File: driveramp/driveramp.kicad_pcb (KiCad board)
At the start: 2 copper layers, 17 parts, among them J1 SMA, J2 SMA, Q1 MRFE6VS25L

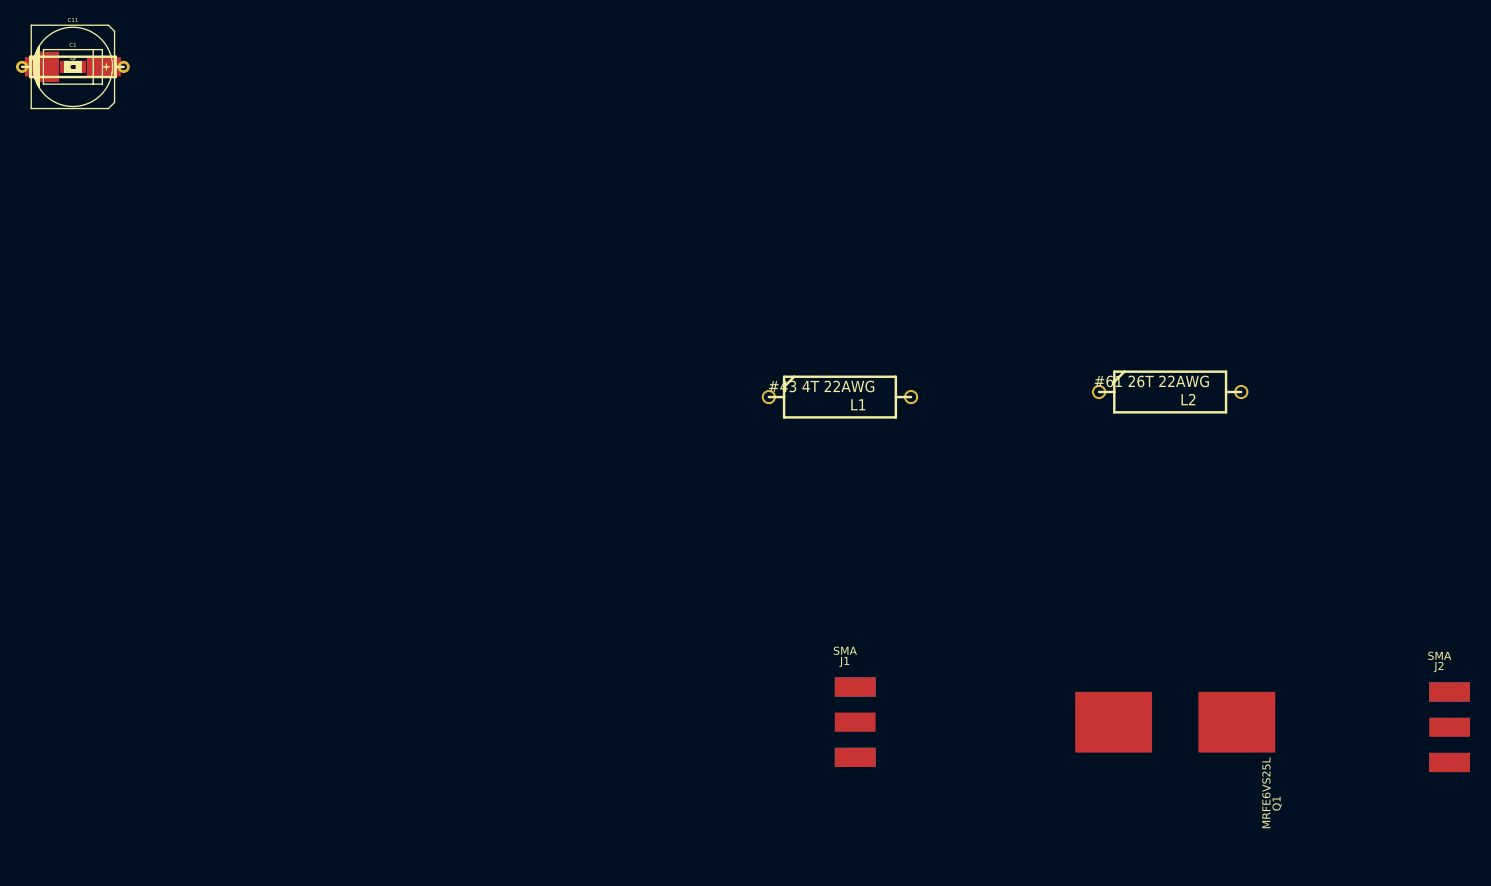
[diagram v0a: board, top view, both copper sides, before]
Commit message: modified trace width classes
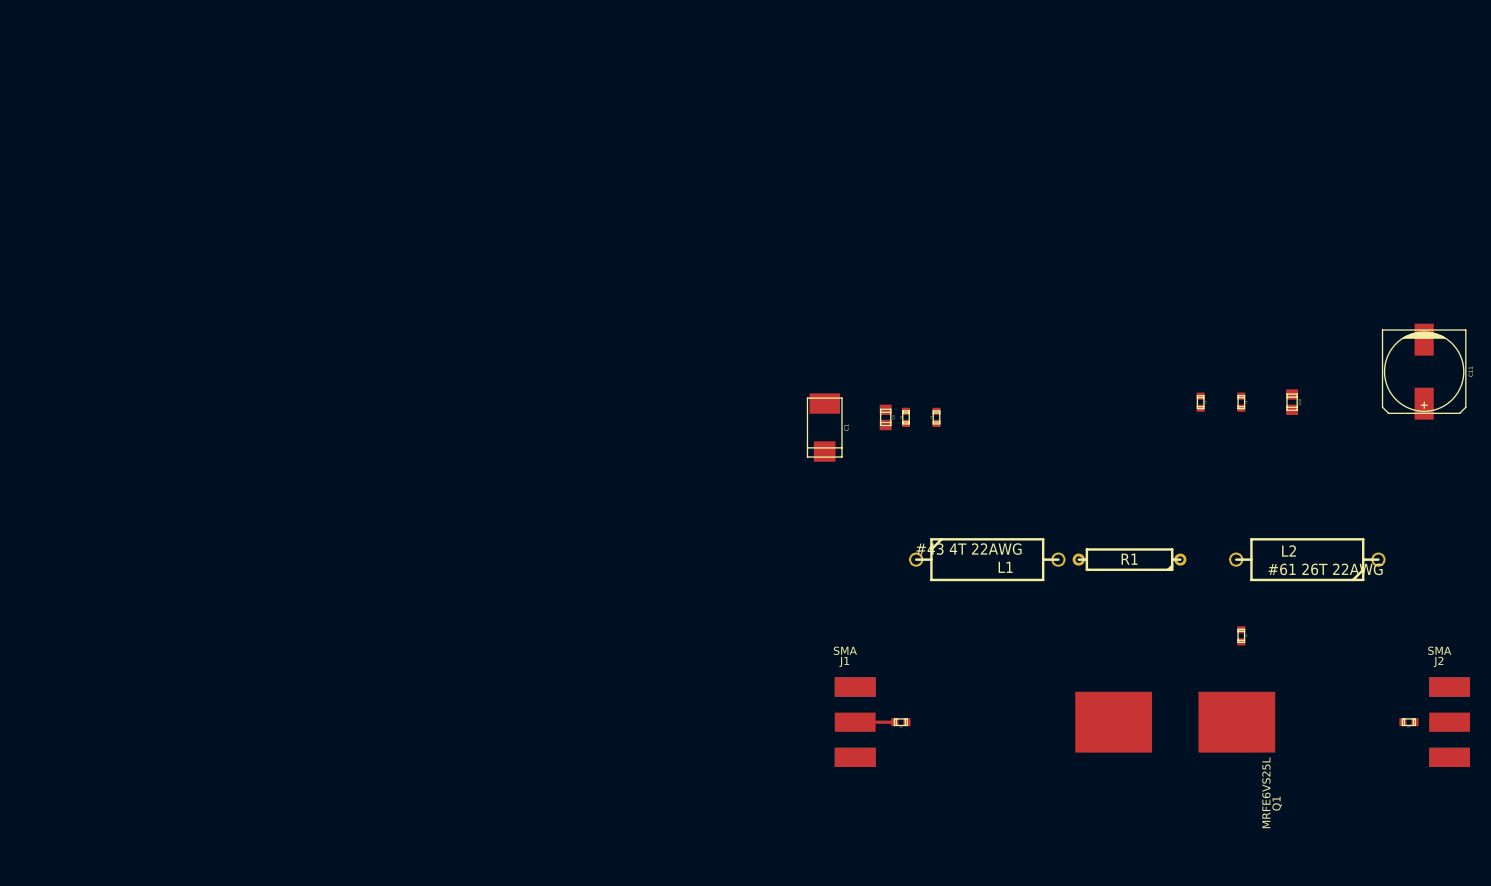
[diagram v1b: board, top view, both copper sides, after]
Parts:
- moved C7 186.0 mm to (167.0, 81.9), turned to 180 degrees
- moved C11 173.2 mm to (168.9, 38.1), turned to 270 degrees
- moved C6 162.4 mm to (146.1, 71.1), turned to 270 degrees
- moved C10 158.1 mm to (152.4, 41.9), turned to 270 degrees
- moved C8 151.9 mm to (146.1, 41.9), turned to 270 degrees
- moved C9 147.1 mm to (141.0, 41.9), turned to 270 degrees
- moved R1 145.7 mm to (132.1, 61.6), turned to 180 degrees
- moved C5 132.0 mm to (103.5, 81.9), turned to 180 degrees
- moved C4 116.5 mm to (108.0, 43.8), turned to 90 degrees
- moved C2 113.0 mm to (104.1, 43.8), turned to 90 degrees
- moved C3 110.6 mm to (101.6, 43.8), turned to 270 degrees
- moved C1 104.2 mm to (94.0, 45.1), turned to 270 degrees
- moved L1 27.4 mm to (114.3, 61.6)
- moved L2 27.1 mm to (154.3, 61.6), turned to 180 degrees
- moved J2 0.63 mm to (172.1, 81.9)
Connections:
- net N-000004 renamed /vbias
- C10 pad 1: N-000003 (its old number) -> /vsupply
- C11 pad 1: N-000003 (its old number) -> /vsupply
- C8 pad 1: N-000003 (its old number) -> /vsupply
- C9 pad 1: N-000003 (its old number) -> /vsupply
- L2 pad 1: N-000003 (its old number) -> /vsupply
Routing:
- net N-000001: track 0.00 -> 4.96 mm
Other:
- copper layers 2 -> 4
- net class 50 Ohm added: clearance 0.8, trace_width 0.4, via_dia 0.889, via_drill 0.635
- net class MRF Feed added: clearance 0.254, trace_width 1.6, via_dia 0.889, via_drill 0.635
- net class Power added: clearance 0.254, trace_width 2, via_dia 0.889, via_drill 0.635

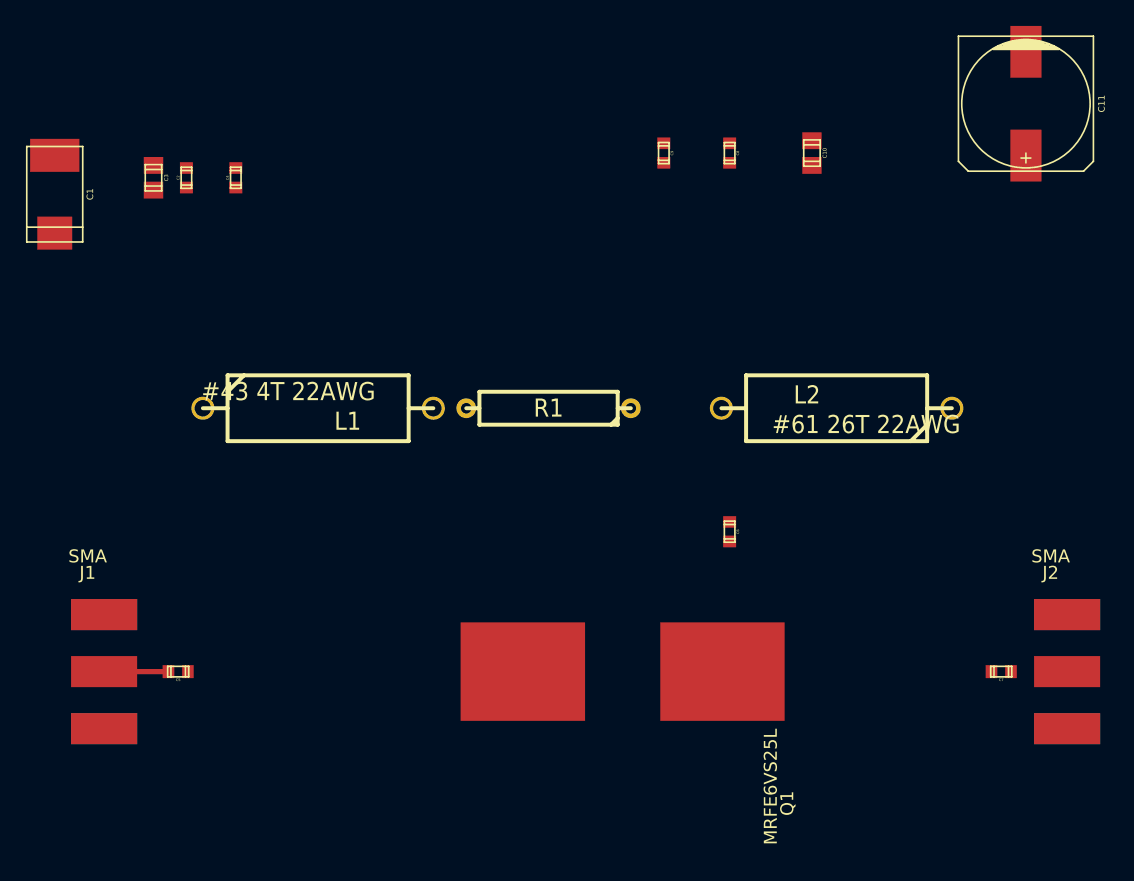
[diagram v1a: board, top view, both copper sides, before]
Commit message: component placement
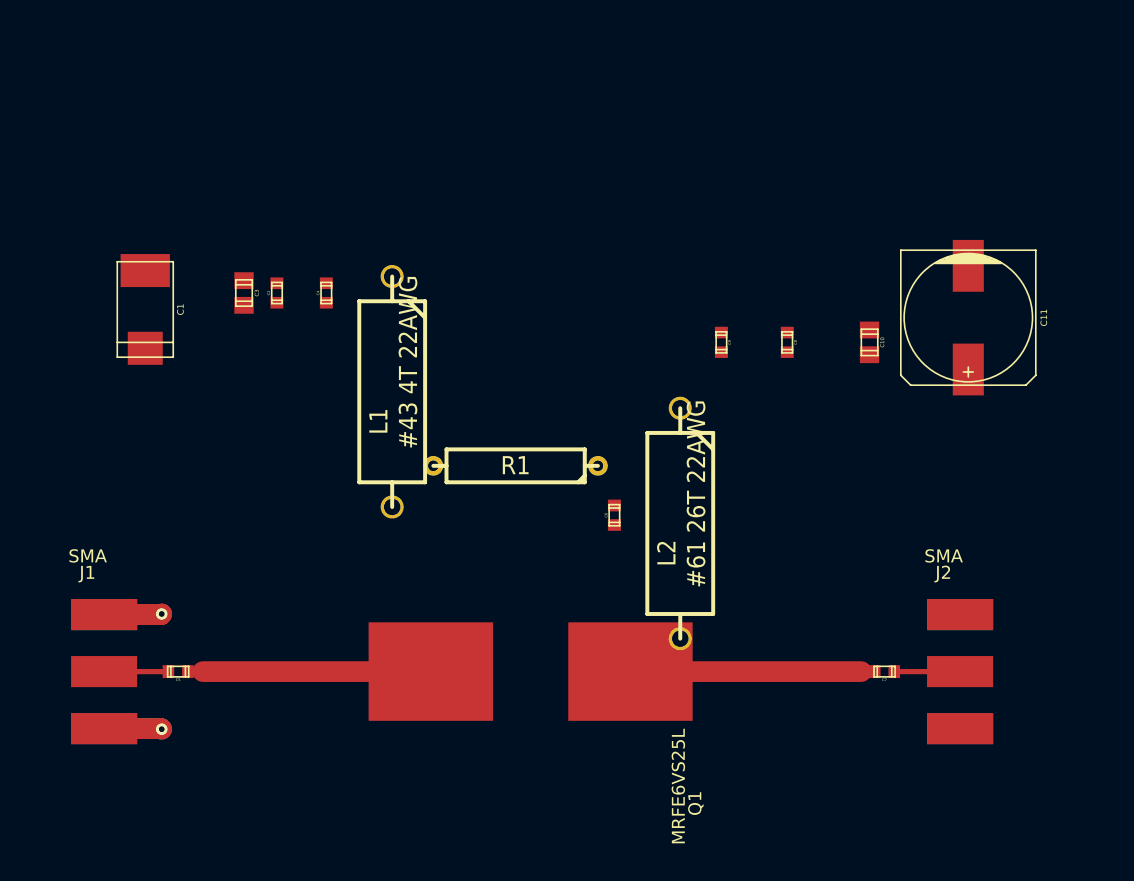
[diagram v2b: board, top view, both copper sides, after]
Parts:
- moved C11 17.1 mm to (164.5, 54.6)
- moved C10 15.3 mm to (156.8, 56.5)
- moved C8 15.3 mm to (150.5, 56.5)
- moved C9 15.3 mm to (145.4, 56.5)
- moved L2 15.0 mm to (142.2, 70.5), turned to 270 degrees
- moved C1 11.3 mm to (101.0, 54.0)
- moved C2 11.3 mm to (111.1, 52.7)
- moved C3 11.3 mm to (108.6, 52.7)
- moved C4 11.3 mm to (114.9, 52.7)
- moved C7 9.00 mm to (158.0, 81.9)
- moved C6 8.98 mm to (137.2, 69.8), turned to 90 degrees
- moved J2 8.25 mm to (163.8, 81.9)
- moved Q1 7.09 mm to (130.7, 81.9)
- moved L1 5.85 mm to (120.0, 60.3), turned to 270 degrees
- moved R1 5.12 mm to (129.5, 66.0)
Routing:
- net GND: track 0.00 -> 22.3 mm, vias 0 -> 2
- net N-000007: track 0.00 -> 18.8 mm
- net N-000008: track 0.00 -> 18.7 mm
- net N-000002: track 0.00 -> 5.08 mm
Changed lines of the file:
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@@
   (general
     (links 32)
-    (no_connects 31)
+    (no_connects 25)
     (area 90.13962 30.966827 175.86188 97.235555)
     (thickness 1.6)
     (drawings 0)
-    (tracks 1)
+    (tracks 17)
     (zones 0)
     (modules 17)
@@
   )
   (setup
-    (last_trace_width 2)
+    (last_trace_width 0.4)
     (user_trace_width 0.254)
     (user_trace_width 0.4)
@@
   )
   (module sma (layer F.Cu)
-    (at 172.085 81.915)
+    (at 163.83 81.915)
     (fp_text reference J2 (at -1.27 -7.62) (layer F.SilkS)
       (effects (font (size 1 1) (thickness 0.15)))
@@
   )
   (module R7 (layer F.Cu)
-    (at 114.3 61.595)
+    (at 120.015 60.325 270)
     (descr "Resitance 7 pas")
     (tags R)
     (autoplace_cost180 10)
-    (fp_text reference L1 (at 2.286 1.016) (layer F.SilkS)
+    (fp_text reference L1 (at 2.286 1.016 270) (layer F.SilkS)
       (effects (font (size 1.397 1.27) (thickness 0.2032)))
     )
-    (fp_text value "#43 4T 22AWG" (at -2.286 -1.27) (layer F.SilkS)
+    (fp_text value "#43 4T 22AWG" (at -2.286 -1.27 270) (layer F.SilkS)
       (effects (font (size 1.397 1.27) (thickness 0.2032)))
     )
@@
     (fp_line (start -6.985 -2.54) (end -6.985 2.54) (layer F.SilkS) (width 0.3048))
     (fp_line (start -8.89 0) (end -6.985 0) (layer F.SilkS) (width 0.3048))
-    (pad 1 thru_hole circle (at -8.89 0) (size 1.778 1.778) (drill 1.27)
+    (pad 1 thru_hole circle (at -8.89 0 270) (size 1.778 1.778) (drill 1.27)
       (layers *.Cu *.Mask F.SilkS)
       (net 1 /vbias)
     )
-    (pad 2 thru_hole circle (at 8.89 0) (size 1.778 1.778) (drill 1.27)
+    (pad 2 thru_hole circle (at 8.89 0 270) (size 1.778 1.778) (drill 1.27)
       (layers *.Cu *.Mask F.SilkS)
       (net 6 N-000003)
@@
   )
   (module R7 (layer F.Cu)
-    (at 154.305 61.595 180)
+    (at 142.24 70.485 270)
     (descr "Resitance 7 pas")
     (tags R)
     (autoplace_cost180 10)
-    (fp_text reference L2 (at 2.286 1.016 180) (layer F.SilkS)
+    (fp_text reference L2 (at 2.286 1.016 270) (layer F.SilkS)
       (effects (font (size 1.397 1.27) (thickness 0.2032)))
     )
-    (fp_text value "#61 26T 22AWG" (at -2.286 -1.27 180) (layer F.SilkS)
+    (fp_text value "#61 26T 22AWG" (at -2.286 -1.27 270) (layer F.SilkS)
       (effects (font (size 1.397 1.27) (thickness 0.2032)))
     )
@@
     (fp_line (start -6.985 -2.54) (end -6.985 2.54) (layer F.SilkS) (width 0.3048))
     (fp_line (start -8.89 0) (end -6.985 0) (layer F.SilkS) (width 0.3048))
-    (pad 1 thru_hole circle (at -8.89 0 180) (size 1.778 1.778) (drill 1.27)
+    (pad 1 thru_hole circle (at -8.89 0 270) (size 1.778 1.778) (drill 1.27)
       (layers *.Cu *.Mask F.SilkS)
       (net 2 /vsupply)
     )
-    (pad 2 thru_hole circle (at 8.89 0 180) (size 1.778 1.778) (drill 1.27)
+    (pad 2 thru_hole circle (at 8.89 0 270) (size 1.778 1.778) (drill 1.27)
       (layers *.Cu *.Mask F.SilkS)
       (net 7 N-000007)
@@
   )
   (module R5 (layer F.Cu)
-    (at 132.08 61.595 180)
+    (at 129.54 66.04 180)
     (descr "Resistance 5 pas")
     (tags R)
@@
   )
   (module NI360 (layer F.Cu)
-    (at 137.795 81.915 270)
+    (at 130.7 81.915 270)
     (fp_text reference Q1 (at 10.16 -12.7 270) (layer F.SilkS)
       (effects (font (size 1 1) (thickness 0.15)))
@@
   )
   (module c_tant_D (layer F.Cu)
-    (at 93.98 45.085 270)
+    (at 100.965 53.975 270)
     (descr "SMT capacitor, tantalum size D")
     (fp_text reference C1 (at 0 -2.7305 270) (layer F.SilkS)
@@
   )
   (module c_elec_10x10 (layer F.Cu)
-    (at 168.91 38.1 270)
+    (at 164.465 54.61 270)
     (descr "SMT capacitor, aluminium electrolytic, 10x10")
     (fp_text reference C11 (at 0 -5.842 270) (layer F.SilkS)
@@
   )
   (module c_0805 (layer F.Cu)
-    (at 152.4 41.91 270)
+    (at 156.845 56.515 270)
     (descr "SMT capacitor, 0805")
     (fp_text reference C10 (at 0 -0.9906 270) (layer F.SilkS)
@@
   )
   (module c_0805 (layer F.Cu)
-    (at 101.6 43.815 270)
+    (at 108.585 52.705 270)
     (descr "SMT capacitor, 0805")
     (fp_text reference C3 (at 0 -0.9906 270) (layer F.SilkS)
@@
   )
   (module c_0603 (layer F.Cu)
-    (at 167.005 81.915 180)
+    (at 158 81.915 180)
     (descr "SMT capacitor, 0603")
     (fp_text reference C7 (at 0 -0.635 180) (layer F.SilkS)
@@
   )
   (module c_0603 (layer F.Cu)
-    (at 146.05 41.91 270)
+    (at 150.495 56.515 270)
     (descr "SMT capacitor, 0603")
     (fp_text reference C8 (at 0 -0.635 270) (layer F.SilkS)
@@
   )
   (module c_0603 (layer F.Cu)
-    (at 140.97 41.91 270)
+    (at 145.415 56.515 270)
     (descr "SMT capacitor, 0603")
     (fp_text reference C9 (at 0 -0.635 270) (layer F.SilkS)
@@
   )
   (module c_0603 (layer F.Cu)
-    (at 104.14 43.815 90)
+    (at 111.125 52.705 90)
     (descr "SMT capacitor, 0603")
     (fp_text reference C2 (at 0 -0.635 90) (layer F.SilkS)
@@
   )
   (module c_0603 (layer F.Cu)
-    (at 107.95 43.815 90)
+    (at 114.935 52.705 90)
     (descr "SMT capacitor, 0603")
     (fp_text reference C4 (at 0 -0.635 90) (layer F.SilkS)
@@
   )
   (module c_0603 (layer F.Cu)
-    (at 146.05 71.12 270)
+    (at 137.16 69.85 90)
     (descr "SMT capacitor, 0603")
-    (fp_text reference C6 (at 0 -0.635 270) (layer F.SilkS)
-      (effects (font (size 0.20066 0.20066) (thickness 0.04064)))
-    )
-    (fp_text value 20nF (at 0 0.635 270) (layer F.SilkS) hide
+    (fp_text reference C6 (at 0 -0.635 90) (layer F.SilkS)
+      (effects (font (size 0.20066 0.20066) (thickness 0.04064)))
+    )
+    (fp_text value 20nF (at 0 0.635 90) (layer F.SilkS) hide
       (effects (font (size 0.20066 0.20066) (thickness 0.04064)))
     )
@@
     (fp_line (start 0.8128 0.4064) (end -0.8128 0.4064) (layer F.SilkS) (width 0.127))
     (fp_line (start -0.8128 0.4064) (end -0.8128 -0.4064) (layer F.SilkS) (width 0.127))
-    (pad 1 smd rect (at 0.75184 0 270) (size 0.89916 1.00076)
+    (pad 1 smd rect (at 0.75184 0 90) (size 0.89916 1.00076)
       (layers F.Cu F.Paste F.Mask)
       (net 9 N-000009)
     )
-    (pad 2 smd rect (at -0.75184 0 270) (size 0.89916 1.00076)
+    (pad 2 smd rect (at -0.75184 0 90) (size 0.89916 1.00076)
       (layers F.Cu F.Paste F.Mask)
       (net 7 N-000007)
@@
     )
   )
-  (segment (start 97.79 81.915) (end 102.75316 81.915) (width 0.4) (layer F.Cu) (net 4) (status C00000))
+  (segment (start 97.79 77.515) (end 102.19 77.515) (width 1.6) (layer B.Cu) (net 3))
+  (segment (start 97.79 77.515) (end 102.19 77.515) (width 1.6) (layer F.Cu) (net 3))
+  (segment (start 102.19 77.515) (end 102.235 77.47) (width 1.6) (layer F.Cu) (net 3))
+  (segment (start 102.19 77.515) (end 102.235 77.47) (width 1.6) (layer F.Cu) (net 3))
+  (via (at 102.235 77.47) (size 0.889) (layers F.Cu B.Cu) (net 3))
+  (segment (start 97.79 86.315) (end 102.19 86.315) (width 1.6) (layer F.Cu) (net 3))
+  (segment (start 102.19 86.315) (end 102.235 86.36) (width 1.6) (layer B.Cu) (net 3))
+  (via (at 102.235 86.36) (size 0.889) (layers F.Cu B.Cu) (net 3))
+  (segment (start 102.19 86.315) (end 97.79 86.315) (width 1.6) (layer B.Cu) (net 3))
+  (segment (start 102.19 86.315) (end 102.235 86.36) (width 1.6) (layer F.Cu) (net 3))
+  (segment (start 97.79 77.515) (end 102.19 77.515) (width 1.6) (layer F.Cu) (net 3))
+  (segment (start 97.79 81.915) (end 102.75316 81.915) (width 0.4) (layer F.Cu) (net 4))
+  (segment (start 158.75184 81.915) (end 163.83 81.915) (width 0.4) (layer F.Cu) (net 5))
+  (segment (start 157.24816 81.915) (end 156.21 81.915) (width 0.4) (layer F.Cu) (net 7))
+  (segment (start 156.21 81.915) (end 138.4 81.915) (width 1.6) (layer F.Cu) (net 7))
+  (segment (start 104.25684 81.915) (end 105.41 81.915) (width 0.4) (layer F.Cu) (net 8))
+  (segment (start 105.41 81.915) (end 123 81.915) (width 1.6) (layer F.Cu) (net 8))
 )
